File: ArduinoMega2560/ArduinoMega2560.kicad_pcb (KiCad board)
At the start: 2 copper layers, 101.6 x 53.3 mm, 74 parts, among them J1 Conn_02x08, J2 Conn_02x08, J3 PINHD_1x2_Male, J4 PINHD_1x2_Male, J5 Conn_02x08, J6 PINHD_2x2_Male, SW1 Push_Button, T1 PMV48XP_215, U1 ATmega2560-16A, U2 ATmega8U2-A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

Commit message: Update
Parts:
- removed J5: Conn_02x08, PCM_4ms_Connector:Pins_2x08_2.54mm_TH
- moved R1 25.2 mm to (120.2, 127.9), turned to 90 degrees
- moved Y1 19.3 mm to (117.6, 125.1), turned to 180 degrees
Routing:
- net /PH5: track 4.25 -> 56.6 mm, vias 0 -> 2
- net /PH6: track 7.44 -> 57.1 mm, vias 0 -> 2
- net /PG5: track 6.56 -> 55.7 mm, vias 0 -> 2
- net Net-(U1-PE3): track 6.48 -> 55.3 mm, vias 0 -> 2
- net /PH4: track 5.94 -> 53.3 mm, vias 0 -> 2
- net Net-(U1-PE4): track 6.44 -> 53.8 mm, vias 0 -> 2
- net Net-(U1-PE5): track 6.68 -> 53.9 mm, vias 0 -> 2
- net /PH3: track 6.72 -> 52.7 mm, vias 0 -> 2
- net /PB0: track 0.00 -> 45.8 mm
- net /PB4: track 10.1 -> 55.1 mm, vias 0 -> 2
- net +5V: track 379.5 -> 420.8 mm, vias 16 -> 18
- net /PB5: track 14.7 -> 55.4 mm, vias 0 -> 2
- net /SCL: track 3.44 -> 42.6 mm, vias 0 -> 2
- net /PB2: track 24.4 -> 63.5 mm
- net /PB1: track 28.7 -> 65.3 mm
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
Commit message: Last trace update
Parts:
- moved ICSP1 2.01 mm to (120.8, 111.5)
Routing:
- net /PL6: track 0.00 -> 60.1 mm
- net /PL4: track 0.00 -> 59.1 mm
- net /PL7: track 0.00 -> 58.2 mm
- net /PL2: track 0.00 -> 58.0 mm
- net /PL0: track 0.00 -> 57.1 mm
- net /PL5: track 0.00 -> 56.5 mm
- net /PL3: track 0.00 -> 55.5 mm
- net /PL1: track 0.00 -> 54.5 mm
- net RESET1: track 140.9 -> 169.4 mm
- net +5V: track 420.8 -> 446.8 mm, vias 18 -> 21
- net Net-(U1-XTAL2): track 0.00 -> 24.1 mm
- net Net-(U1-XTAL1): track 0.00 -> 23.7 mm
- net /RXD2: track 52.8 -> 41.0 mm
- net /TXD2: track 49.9 -> 38.2 mm
- net Net-(U1-PE5): track 53.9 -> 45.2 mm
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
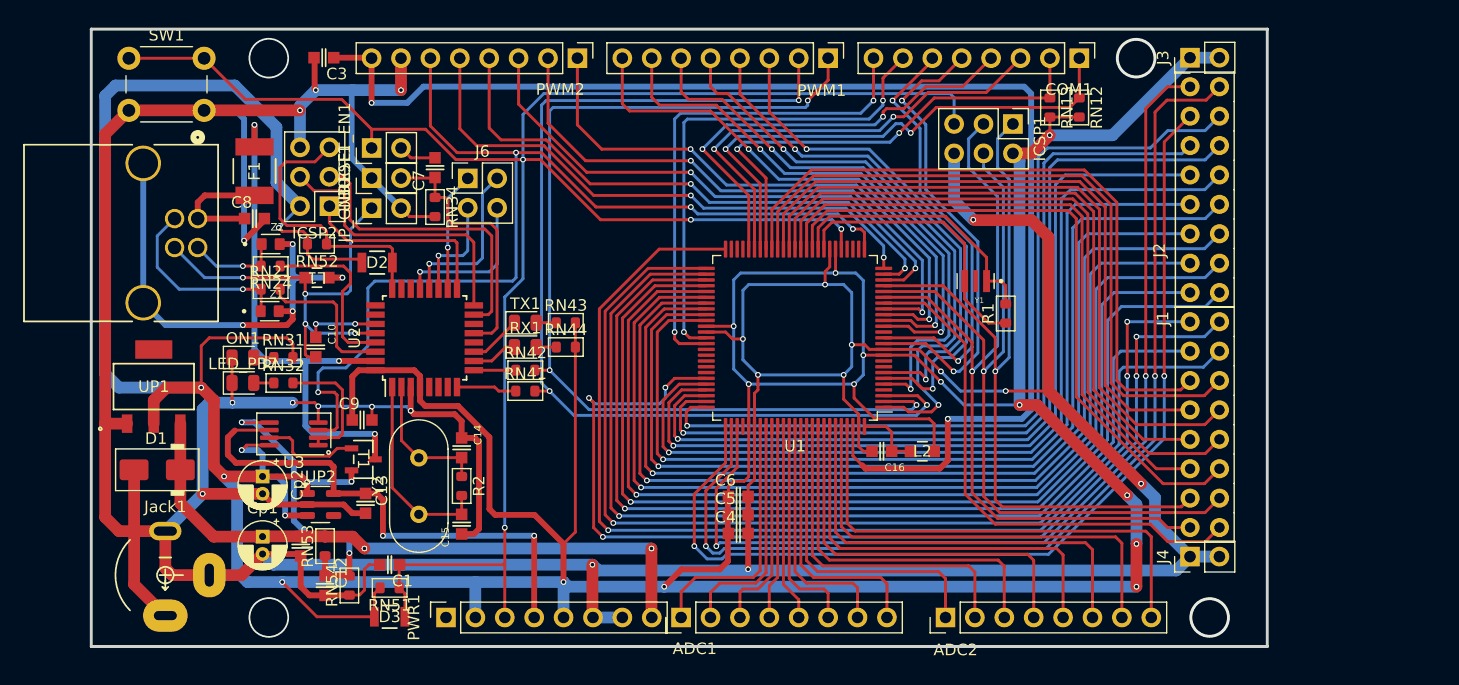
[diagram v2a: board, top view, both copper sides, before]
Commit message: Update footprint and silkscree
next, fixing the trace on the pinheader
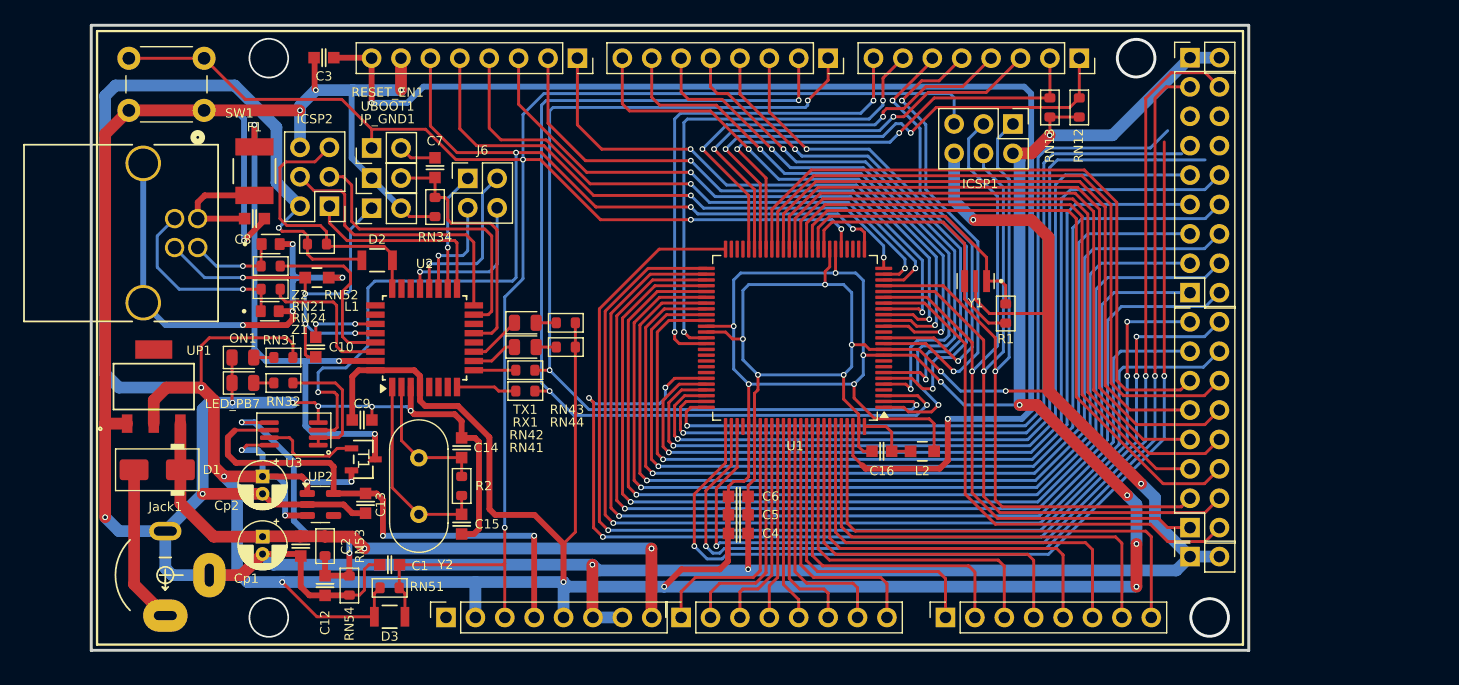
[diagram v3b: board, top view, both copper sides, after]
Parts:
- ADC1, ADC2, COM1, PWM1, PWM2: value PINHD_1x8_Male -> PINHD_1x8_Female; footprint Connector_PinHeader_2.54mm:PinHeader_1x08_P2.54mm_Vertical -> Connector_PinSocket_2.54mm:PinSocket_1x08_P2.54mm_Vertical
- J1, J2: footprint PCM_4ms_Connector:Pins_2x08_2.54mm_TH -> Connector_PinSocket_2.54mm:PinSocket_2x08_P2.54mm_Vertical
- J3, J4: value PINHD_1x2_Male -> PINHD_1x2_Female; footprint Connector_PinHeader_2.54mm:PinHeader_1x02_P2.54mm_Vertical -> Connector_PinSocket_2.54mm:PinSocket_1x02_P2.54mm_Vertical
- moved J1 8.99 mm to (136.1, 146.4)
- moved J2 8.99 mm to (136.1, 126.1)
- moved D2 0.20 mm to (65.9, 123.3)
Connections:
- D1 pad 2: GND -> Net-(D1-A)
- Jack1 pad 1: GND -> Net-(D1-A)
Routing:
- net Net-(D1-A): track 0.00 -> 13.7 mm
- net GND: track 441.3 -> 436.0 mm, vias 21 -> 22
- net /PA3: track 73.2 -> 68.2 mm
- net /PA0: track 85.3 -> 89.3 mm
- net /PA2: track 85.6 -> 82.4 mm
- net /PA1: track 89.1 -> 87.3 mm
- net /PA5: track 76.1 -> 74.4 mm
- net /PA4: track 71.6 -> 70.6 mm
- added copper zone on B.Cu, net GND
- added copper zone on F.Cu, net GND
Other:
- board size 101.6 x 53.3 mm -> 100 x 54 mm

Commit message: Final
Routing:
- net /PA2: track 82.4 -> 88.1 mm
- net /PA4: track 70.6 -> 75.6 mm
- net /PL6: track 60.1 -> 55.4 mm
- net /PG1: track 86.9 -> 91.5 mm
- net /PC7: track 81.2 -> 85.7 mm
- net /PC5: track 83.2 -> 87.6 mm
- net /PA6: track 73.8 -> 78.2 mm
- net /PD7: track 96.4 -> 100.6 mm
- net /PL0: track 57.1 -> 53.5 mm
- net /PC1: track 87.1 -> 90.7 mm
- net /PL4: track 59.1 -> 55.5 mm
- net /PB3: track 65.8 -> 69.3 mm
- net /PC3: track 85.2 -> 88.7 mm
- net /PL2: track 58.0 -> 54.5 mm
- net /PB0: track 45.7 -> 42.1 mm
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
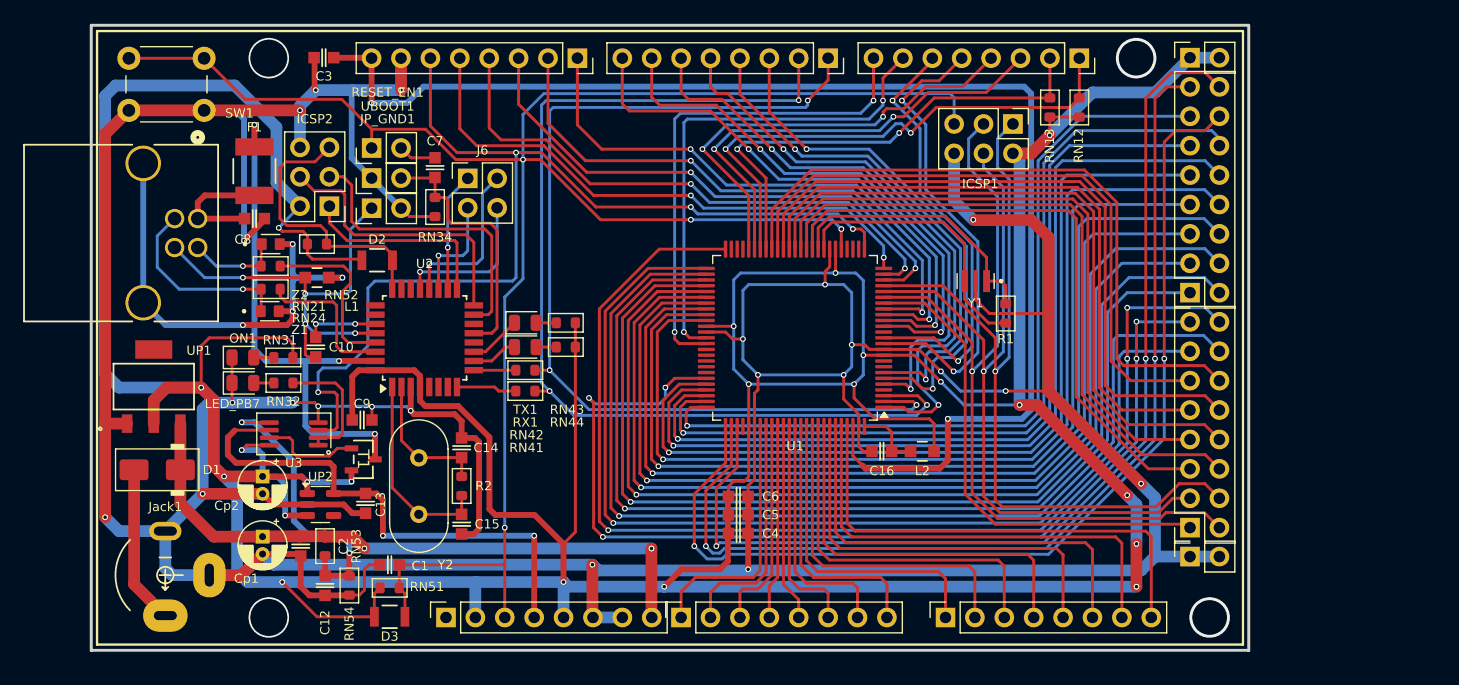
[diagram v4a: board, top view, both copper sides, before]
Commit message: Tuning serial and crystal tracks
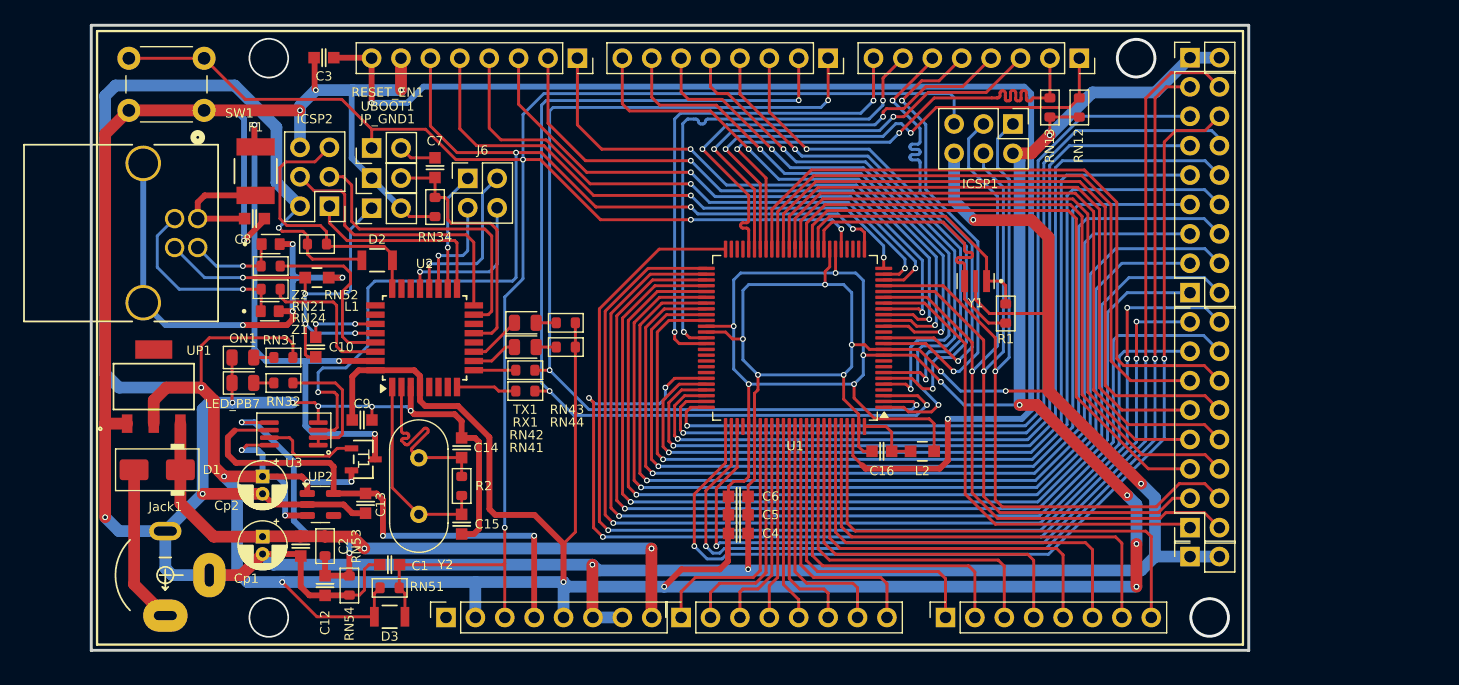
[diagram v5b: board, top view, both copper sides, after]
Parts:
- moved F1 0.10 mm to (55.4, 115.6)
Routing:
- net /ATmega8U2-MU/XT2: track 12.1 -> 17.2 mm
- net /SDA: track 42.0 -> 46.3 mm
- net /TXD2: track 38.2 -> 41.0 mm
- net Net-(U1-XTAL2): track 24.1 -> 26.3 mm
- net /TXD1: track 38.7 -> 39.8 mm
- net RXD0: track 87.2 -> 88.0 mm
- net /RXD3: track 42.8 -> 43.4 mm

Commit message: Update Eth
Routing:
- net /PH3: track 46.1 -> 47.8 mm
- net Net-(U1-PE3): track 48.8 -> 50.5 mm
- net /PH4: track 47.2 -> 48.9 mm
- net /PG5: track 51.2 -> 52.9 mm
- net Net-(U1-PE5): track 45.2 -> 46.2 mm
- net /PH5: track 50.3 -> 51.3 mm
- net /PB6: track 48.9 -> 49.5 mm
